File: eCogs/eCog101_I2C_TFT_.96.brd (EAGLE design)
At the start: 47.5 x 28 mm, 4 parts

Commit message: Updated to latest eCog Library
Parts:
- ECOG: value ECOG_BUSES_ROWECOG_BUSES_SMD -> ECOG_BUSES_ROWSURFACEMOUNT
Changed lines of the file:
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@@
 </autorouter>
 <elements>
-<element name="ECOG" library="eCogs" package="ECOG_BUSES_SMD" value="ECOG_BUSES_ROWECOG_BUSES_SMD" x="0" y="0" smashed="yes">
+<element name="ECOG" library="eCogs" package="ECOG_BUSES_SMD" value="ECOG_BUSES_ROWSURFACEMOUNT" x="0" y="0" smashed="yes">
 <attribute name="DIGIKEY" value="S1013EC-10-ND" x="0" y="0" size="1.778" layer="27" display="off"/>
 </element>

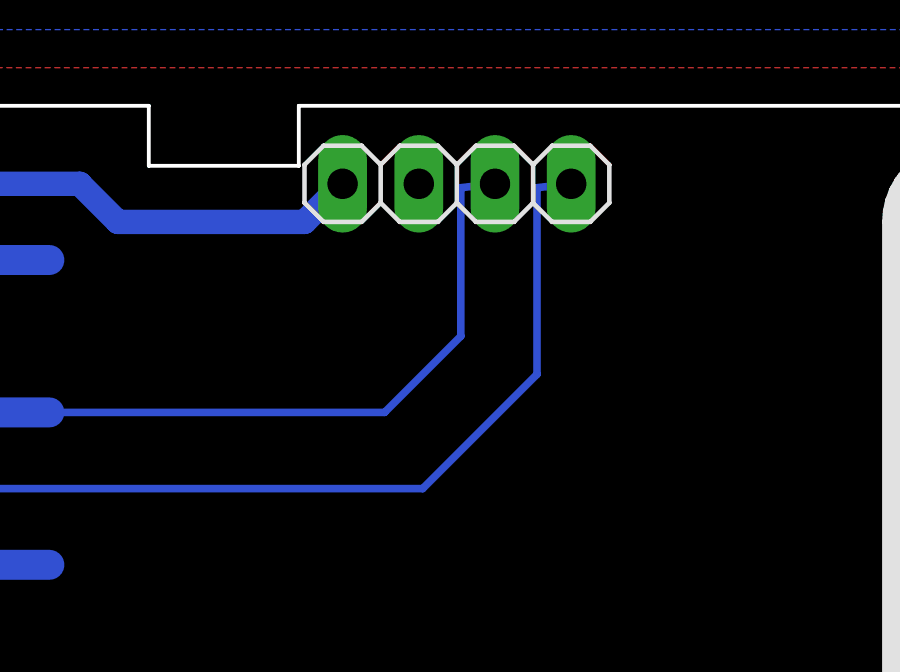
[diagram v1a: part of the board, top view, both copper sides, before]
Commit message: Fix silkscreen
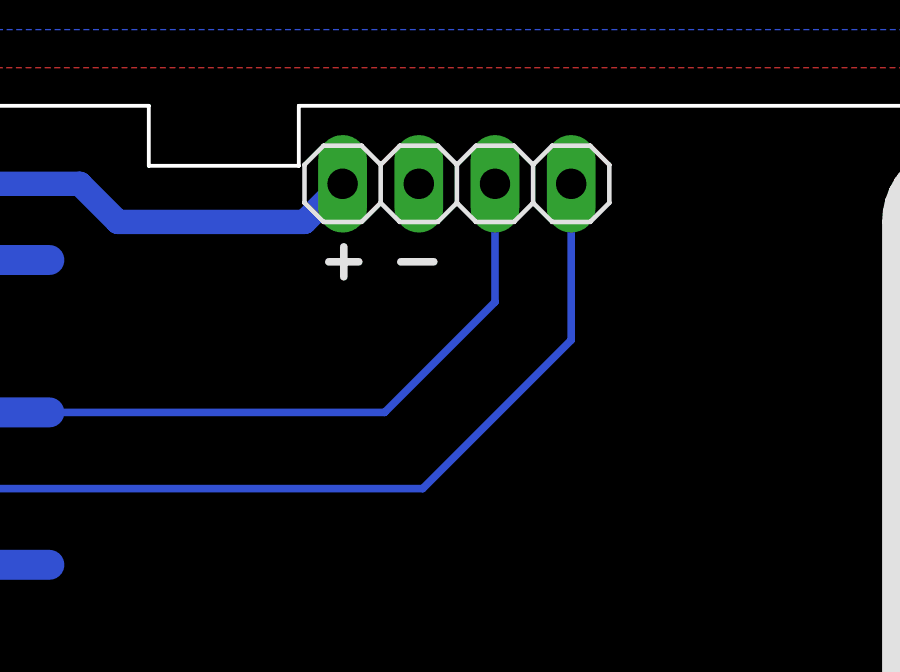
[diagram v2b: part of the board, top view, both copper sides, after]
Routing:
- net N$1: track 22.1 -> 21.6 mm
- net N$2: track 29.5 -> 29.0 mm
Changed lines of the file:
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@@
 <setting verticaltext="up"/>
 </settings>
-<grid distance="0.05" unitdist="inch" unit="inch" style="lines" multiple="1" display="yes" altdistance="0.005" altunitdist="inch" altunit="inch"/>
+<grid distance="1" unitdist="mm" unit="mm" style="lines" multiple="1" display="yes" altdistance="0.1" altunitdist="mm" altunit="mm"/>
 <layers>
 <layer number="1" name="Top" color="4" fill="1" visible="yes" active="yes"/>
@@
 <wire x1="39.824" y1="2.71" x2="39.824" y2="7.1412" width="0.254" layer="21"/>
 <wire x1="39.824" y1="7.5358" x2="39.824" y2="25.23" width="0.254" layer="21"/>
+<wire x1="23.4" y1="22.8" x2="24.5" y2="22.8" width="0.254" layer="21"/>
+<wire x1="21" y1="22.8" x2="21.5" y2="22.8" width="0.254" layer="21"/>
+<wire x1="21.5" y1="22.8" x2="22" y2="22.8" width="0.254" layer="21"/>
+<wire x1="21.5" y1="22.8" x2="21.5" y2="23.3" width="0.254" layer="21"/>
+<wire x1="21.5" y1="22.8" x2="21.5" y2="22.3" width="0.254" layer="21"/>
 </plain>
 <attributes>
@@
 <contactref element="JP1" pad="4"/>
 <wire x1="7.337490625" y1="15.24" x2="24.13" y2="15.24" width="0.254" layer="16"/>
-<wire x1="24.13" y1="15.24" x2="27.94" y2="19.05" width="0.254" layer="16"/>
-<wire x1="27.94" y1="19.05" x2="27.94" y2="25.27" width="0.254" layer="16"/>
-<wire x1="27.94" y1="25.27" x2="29.08" y2="25.4" width="0.254" layer="16"/>
+<wire x1="24.13" y1="15.24" x2="29.08" y2="20.19" width="0.254" layer="16"/>
+<wire x1="29.08" y1="25.4" x2="29.08" y2="20.19" width="0.254" layer="16"/>
 </signal>
 <signal name="N$1">
@@
 <contactref element="ECOG" pad="I2C-SCL"/>
 <wire x1="10.436290625" y1="17.78" x2="22.86" y2="17.78" width="0.254" layer="16"/>
-<wire x1="22.86" y1="17.78" x2="25.4" y2="20.32" width="0.254" layer="16"/>
-<wire x1="25.4" y1="20.32" x2="25.4" y2="25.27" width="0.254" layer="16"/>
-<wire x1="25.4" y1="25.27" x2="26.54" y2="25.4" width="0.254" layer="16"/>
+<wire x1="22.86" y1="17.78" x2="26.54" y2="21.46" width="0.254" layer="16"/>
+<wire x1="26.54" y1="25.4" x2="26.54" y2="21.46" width="0.254" layer="16"/>
 </signal>
 </signals>
